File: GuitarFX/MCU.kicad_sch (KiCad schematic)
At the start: 1 part, among them U2 STM32H733VGTx

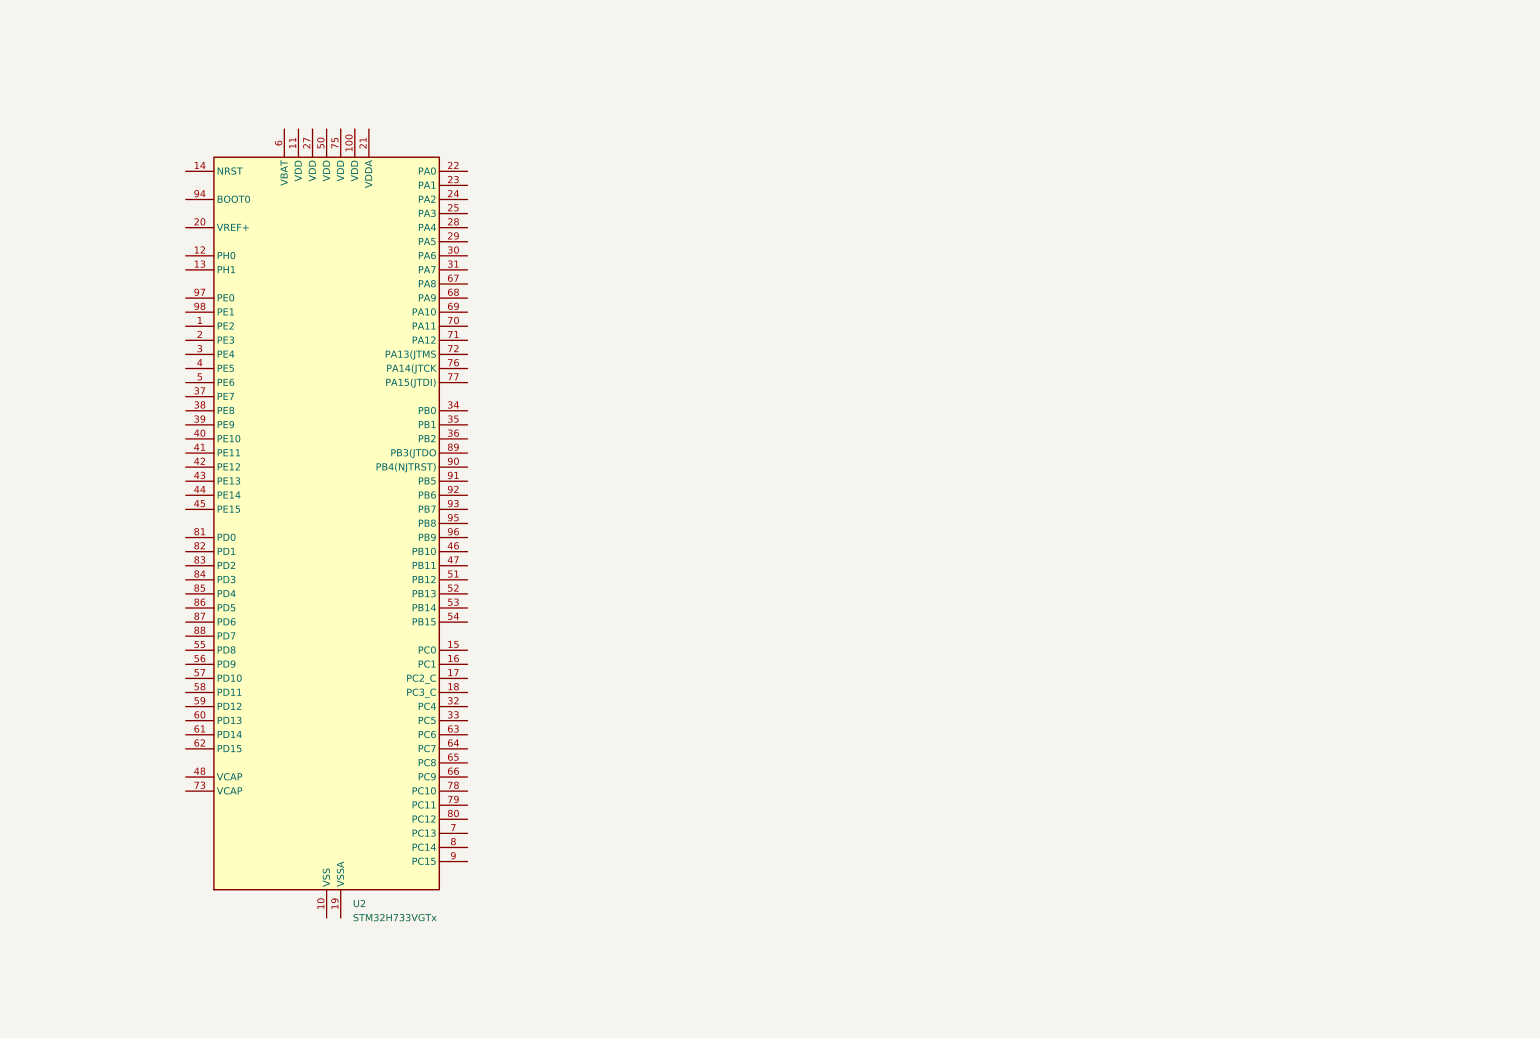
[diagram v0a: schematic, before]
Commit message: Added decuopling capacitors and filtering to MCU
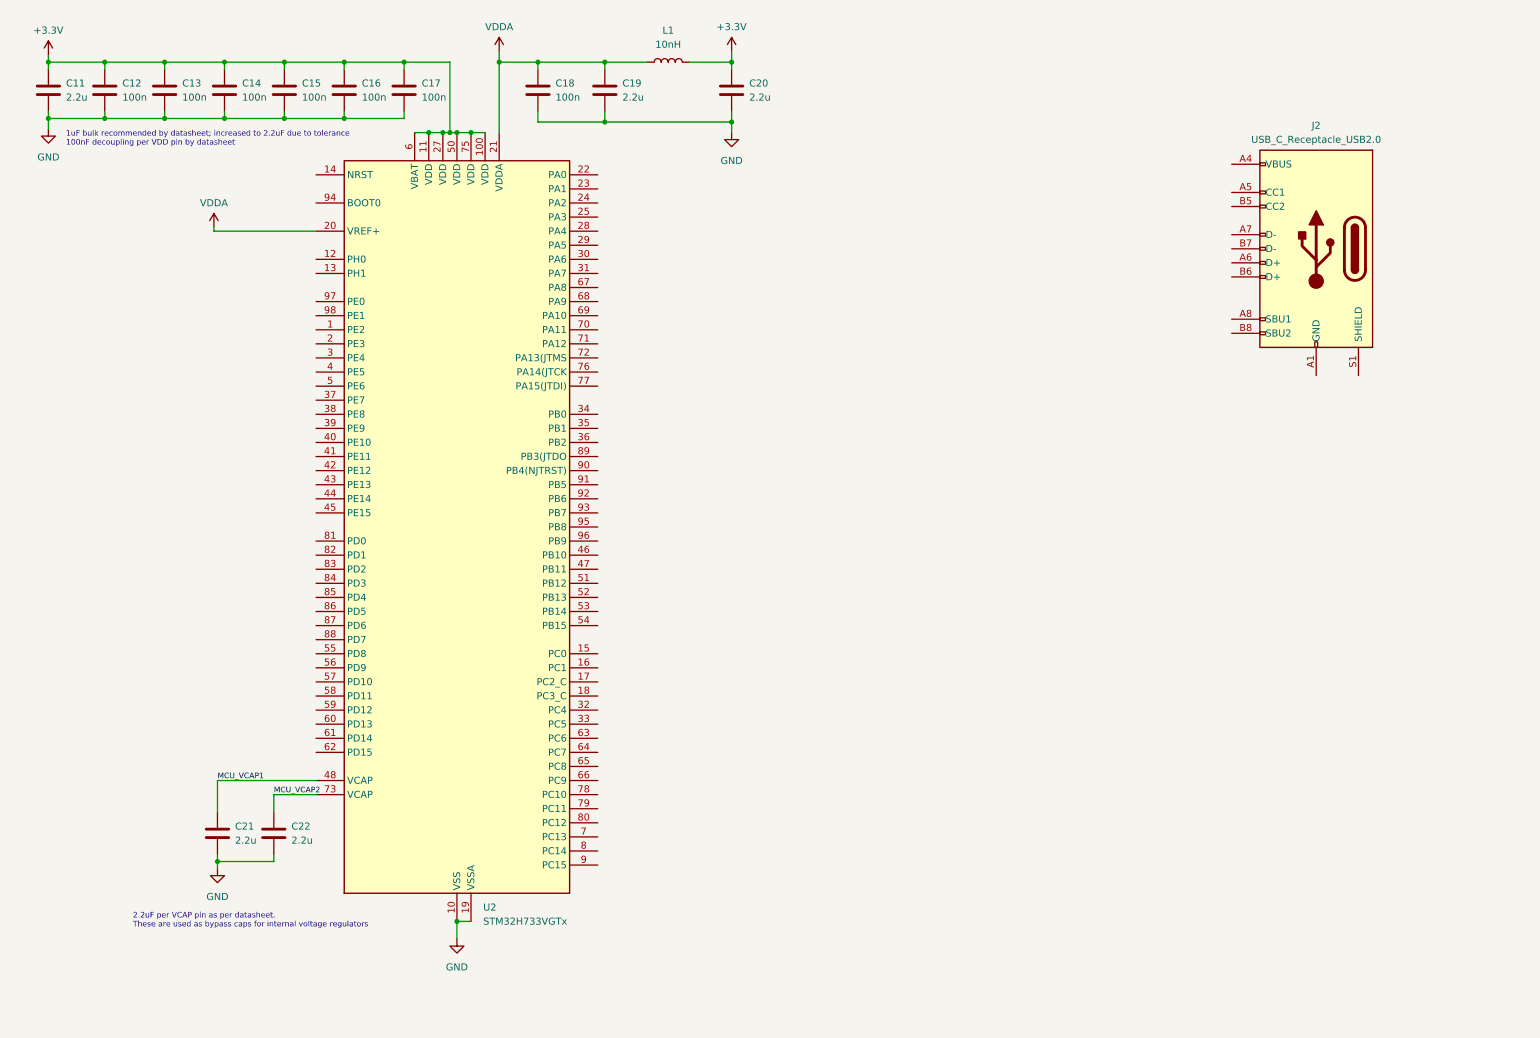
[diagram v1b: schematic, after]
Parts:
- added C11, C19, C20, C21, C22: 2.2u, symbol Device:C
- added C12, C13, C14, C15, C16, C17, C18: 100n, symbol Device:C
- added J2: USB_C_Receptacle_USB2.0, symbol Connector:USB_C_Receptacle_USB2.0
- added L1: 10nH, symbol Device:L
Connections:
- net GND: now reaches U2.10 (VSS), U2.26 (VSS), U2.49 (VSS), U2.74 (VSS), U2.99 (VSS)
- net GND: now also U2.19 (VSSA), C11.2, C12.2, C13.2, C14.2, C15.2, C16.2, C17.2, C18.2, C19.2, C20.2, C21.2, C22.2
- net +3.3V: now reaches U2.100 (VDD)
- net +3.3V: now also U2.11 (VDD), U2.27 (VDD), U2.50 (VDD), U2.6 (VBAT), U2.75 (VDD), C11.1, C12.1, C13.1, C14.1, C15.1, C16.1, C17.1, C20.1, L1.2
- net VDDA: now reaches U2.20 (VREF+)
- net VDDA: now also U2.21 (VDDA), C18.1, C19.1, L1.1
- net MCU_VCAP1: now reaches U2.48 (VCAP)
- net MCU_VCAP1: now also C21.1
- net MCU_VCAP2: now reaches U2.73 (VCAP)
- net MCU_VCAP2: now also C22.1
- new net: J2.A1 (GND), J2.A12 (GND), J2.B1 (GND), J2.B12 (GND)
- new net: J2.A4 (VBUS), J2.A9 (VBUS), J2.B4 (VBUS), J2.B9 (VBUS)
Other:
- note added: "1uF bulk recommended by datasheet; increased to 2.2uF due to tolerance 100nF decoupling per VDD pin by datasheet"
- note added: "2.2uF per VCAP pin as per datasheet. These are used as bypass caps for internal voltage regulators"
- moved on the sheet: U2

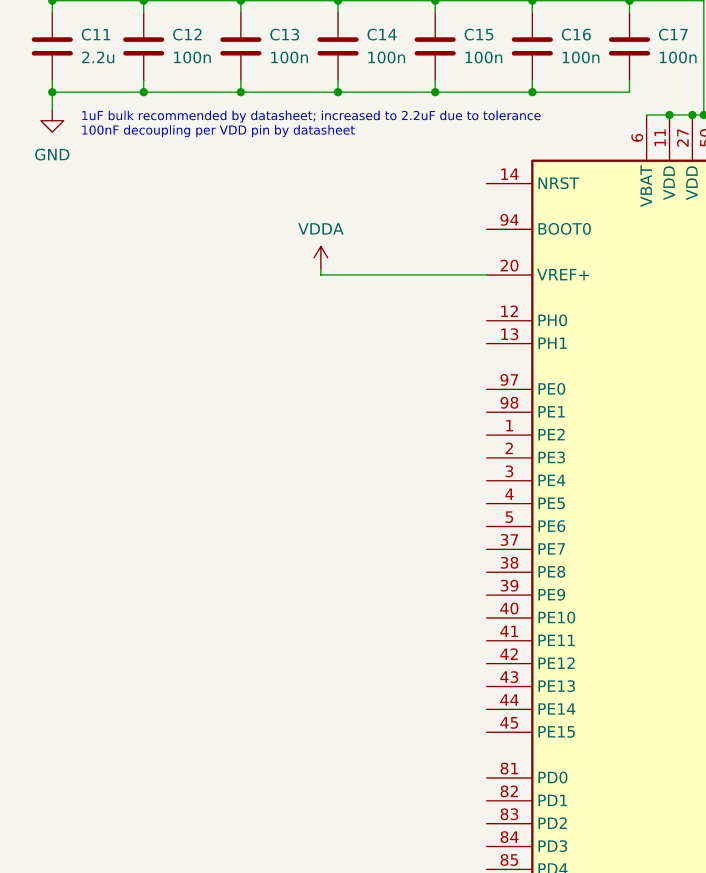
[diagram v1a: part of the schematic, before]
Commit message: Finished crystal oscillator circuit
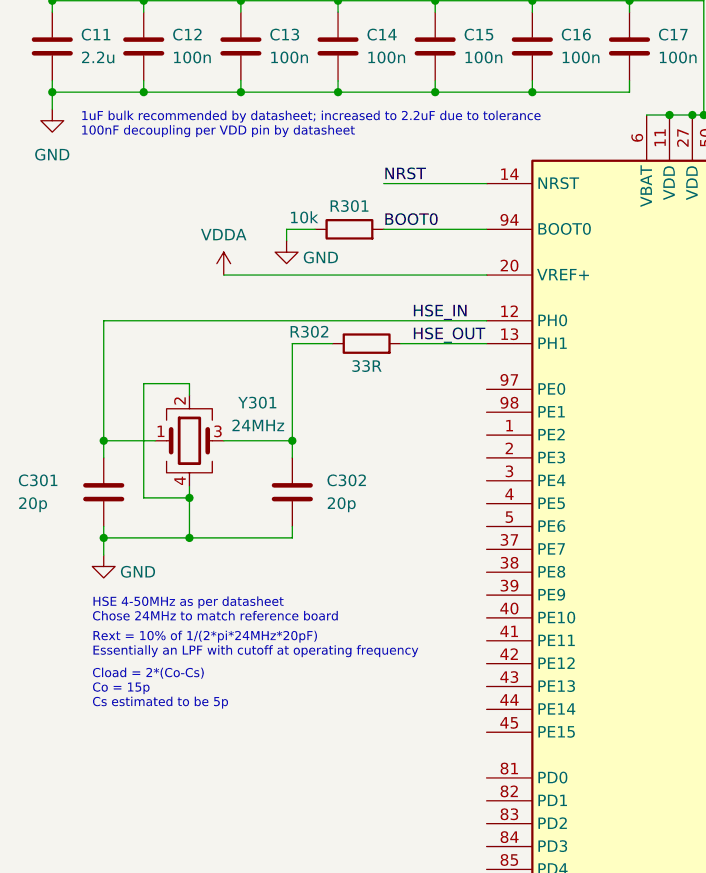
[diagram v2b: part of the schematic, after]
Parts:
- added C301, C302: 20p, symbol Device:C
- added R301: 10k, symbol Device:R
- added R302: 33R, symbol Device:R
- added Y301: 24MHz, symbol Device:Crystal_GND24
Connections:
- net GND: now also C301.2, C302.2, R301.1, Y301.2, Y301.4
- net HSE_IN: now reaches U2.12 (PH0)
- net HSE_IN: now also C301.1, Y301.1
- net HSE_OUT: now reaches U2.13 (PH1)
- net HSE_OUT: now also R302.2
- net NRST: now reaches U2.14 (NRST)
- net BOOT0: now reaches U2.94 (BOOT0)
- net BOOT0: now also R301.2
- new net: C302.1, R302.1, Y301.3
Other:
- note added: "Cload = 2*(Co-Cs) Co = 15p Cs estimated to be 5p"
- note added: "HSE 4-50MHz as per datasheet Chose 24MHz to match reference board"
- note added: "Rext = 10% of 1/(2*pi*24MHz*20pF) Essentially an LPF with cutoff at operating frequency"

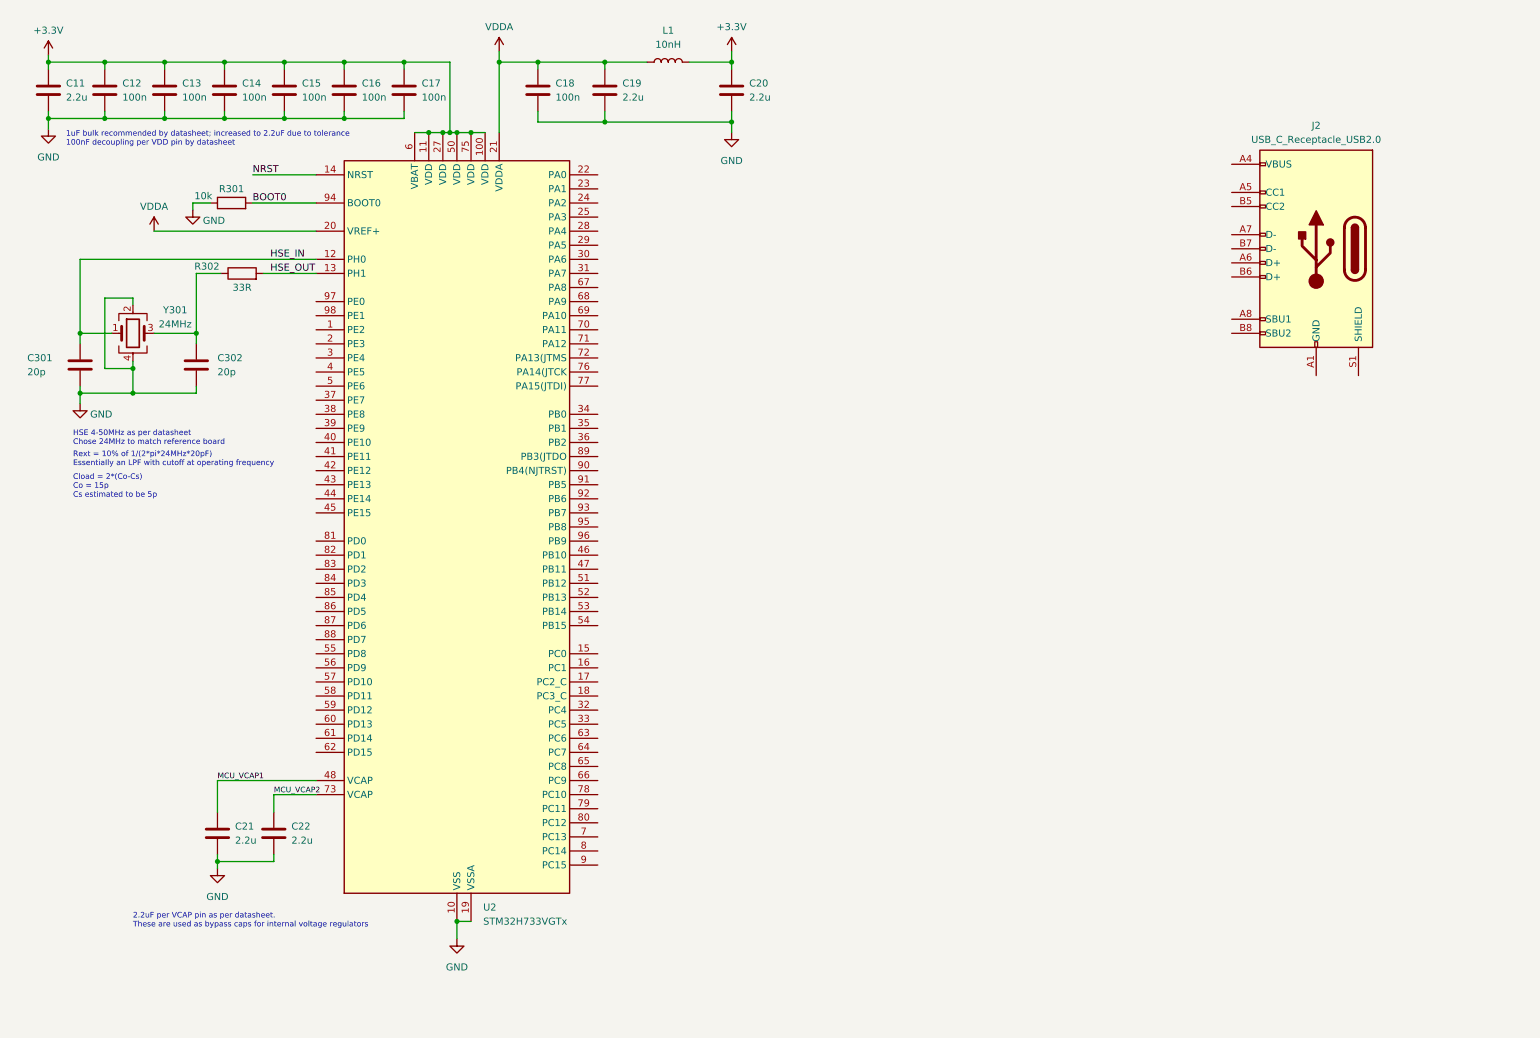
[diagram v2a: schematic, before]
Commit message: Finished tag connect SWD connections on schematic
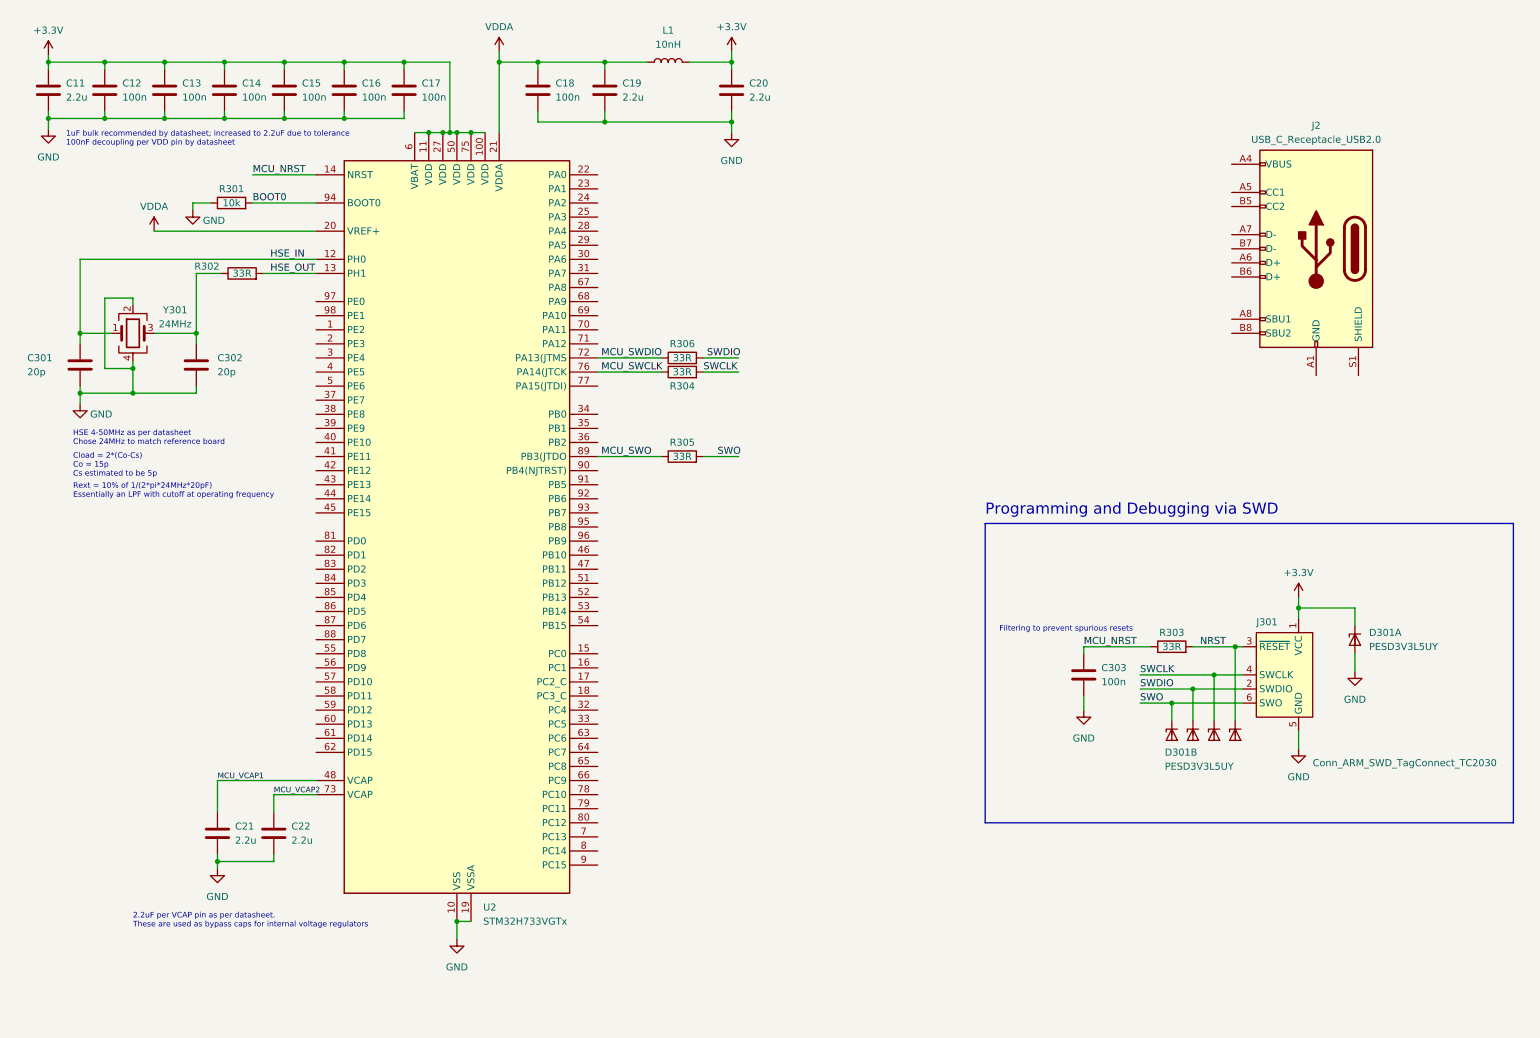
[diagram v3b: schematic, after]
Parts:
- added C303: 100n, symbol Device:C
- added D301: PESD3V3L5UY, Package_TO_SOT_SMD:SOT-363_SC-70-6, symbol Power_Protection:PESD3V3L5UY
- added J301: Conn_ARM_SWD_TagConnect_TC2030, Connector:Tag-Connect_TC2030-IDC-FP_2x03_P1.27mm_Vertical, symbol Connector:Conn_ARM_SWD_TagConnect_TC2030
- added R303, R304, R305, R306: 33R, symbol Device:R
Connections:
- net +3.3V: now also D301.1 (K1), J301.1 (VCC)
- net GND: now also C303.2, D301.2 (A), J301.5 (GND)
- net NRST: now also D301.3 (K2), J301.3 (~{RESET}), R303.2; no longer U2.14 (NRST)
- net MCU_SWDIO: now reaches U2.72 (PA13(JTMS)
- net MCU_SWDIO: now also R306.1
- net MCU_SWCLK: now reaches U2.76 (PA14(JTCK)
- net MCU_SWCLK: now also R304.1
- net MCU_SWO: now reaches U2.89 (PB3(JTDO)
- net MCU_SWO: now also R305.1
- new net MCU_NRST: C303.1, R303.1, U2.14 (NRST)
- new net SWCLK: D301.4 (K3), J301.4 (SWCLK), R304.2
- new net SWDIO: D301.5 (K4), J301.2 (SWDIO), R306.2
- new net SWO: D301.6 (K5), J301.6 (SWO), R305.2
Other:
- note added: "Filtering to prevent spurious resets"
- note added: "Programming and Debugging via SWD"

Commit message: Added USB-C connector to schematic and changed inductors in filters to ferrites
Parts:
- removed C19, C20: 2.2u, symbol Device:C
- removed L1: 10nH, symbol Device:L
- added C304, C305, C306, C307, C308: 100n, symbol Device:C
- added D2: SMAJ15A, Diode_SMD:D_SMA, symbol Diode:SMAJ15A
- added FB301, FB302: 120R, symbol Device:FerriteBead
- added FL301: ACM2012-900-2P-TL002, ACM20129002PTL002, symbol ACM2012-900-2P-TL002:ACM2012-900-2P-TL002
- added R307, R308: 5.1k, symbol Device:R
- added U301: USBLC6-2SC6, Package_TO_SOT_SMD:SOT-23-6, symbol Power_Protection:USBLC6-2SC6
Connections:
- net +3.3V: now also C308.1, FB302.2
- net GND: now also J2.A1 (GND), J2.A12 (GND), J2.B1 (GND), J2.B12 (GND), C304.2, C305.2, C306.2, C307.2, C308.2, D2.2 (A2), R307.2, R308.2, U301.2 (GND)
- net VDDA: now also C307.1, FB302.1
- net USB_FS_D-: now reaches U2.70 (PA11)
- net USB_FS_D-: now also FL301.3
- net USB_FS_D+: now reaches U2.71 (PA12)
- net USB_FS_D+: now also FL301.4
- net VBUS: now reaches J2.A4 (VBUS), J2.A9 (VBUS), J2.B4 (VBUS), J2.B9 (VBUS)
- net VBUS: now also C304.1, C305.1, D2.1 (A1), FB301.1, U301.5 (VBUS)
- net USB_CON_CC1: now reaches J2.A5 (CC1)
- net USB_CON_CC1: now also R307.1
- net USB_CON_D+: now reaches J2.A6 (D+)
- net USB_CON_D+: now also J2.B6 (D+), U301.3 (I/O2)
- net USB_CON_D-: now reaches J2.A7 (D-)
- net USB_CON_D-: now also J2.B7 (D-), U301.1 (I/O1)
- net USB_CON_CC2: now reaches J2.B5 (CC2)
- net USB_CON_CC2: now also R308.1
- new net USB_CMC_D+: FL301.2, U301.4 (I/O2)
- new net USB_CMC_D-: FL301.1, U301.6 (I/O1)
- new net VUSB_FILT: C306.1, FB301.2
- no-connect marks 0 -> 3
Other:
- note added: "5.1k on comm channels for 5V, 500mA"
- note added: "USB-C Connector"
- moved on the sheet: C18, C303, D301A, D301B, J2, J301, R303
